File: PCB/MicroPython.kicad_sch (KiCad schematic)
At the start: 70 parts, among them J1 Conn_01x08, J10 USB4105-GF-A, J11 Micro_SD_Card, J2 Conn_01x08, J3 Conn_01x08, J4 Conn_01x08, J5 Conn_02x04_Odd_Even, J6 Conn_01x08, J7 Conn_01x08, J8 Conn_02x03_Odd_Even, J9 Conn_01x02, Q1 DMP2160UW, SW1 SW_MEC_5E, SW2 SW_MEC_5E, U1 STM32F405RGT6, U2 MCP1700T, U3 MIC2005A-1YM5, U4 FXLS8971CFR1, Y1 12 MHz, Y2 32.768 kHz

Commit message: actualizado/modificado nome de projecto - MicroPython
- nome alterado para estar de acordo com folder de Projecto & Repositório no GitHub
- desenho ainda em desenvolvimento
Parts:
- removed C3: 2u2, Capacitor_SMD:C_0603_1608Metric, symbol Device:C_Small
- C9: now not fitted; now left out of the parts list
- J11: footprint PyBoard FootprintLib:47571-0001_MOL -> MicroPython FootprintLib:47571-0001_MOL
- U1: symbol PyBoard SymbLib:STM32F405RGT6 -> MicroPython SymbLib:STM32F405RGT6
- U4: footprint PyBoard FootprintLib:LQFN-12-3x3mm_P0.65mm -> MicroPython FootprintLib:LQFN-12-3x3mm_P0.65mm; symbol PyBoard SymbLib:FXLS8971CFR1 -> MicroPython SymbLib:FXLS8971CFR1; now not fitted; now left out of the parts list
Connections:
- net PA11-DM renamed USB_N
- net PA12-DP renamed USB_P
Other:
- note added: ". 32kHz crystal used 'only' to SD-Card . since SD-card won't be used, does Crystal needs to be assmbled? . isn't OSC-pins needed to outher micro functionalities?"
- note added: "PA10-ID: USB 2.0 ID with no pin conn on USB-C will create USB fw-trouble?"
- note added: "rest of JTAG & SW debug available on bottom connector Note: LED resistors may need to be removed for debug (tbd) (note from v.1.1) programming pins PA13 PA14 PA15 PB4 connected to LEDs trouble??"
- note removed: "PA10-ID: USB ID sem conn nesta ficha afecta algo com o fw?"
- note removed: "programming pins PA13 PA14 PA15 PB4 connected to LEDs trouble??"
- note removed: "rest of JTAG & SW debug available on bottom connector Note: LED resistors may need to be removed for debug (tbd) (note from v.1.1)"

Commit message: MicroPython v.1.0
MicroPython v.1.0
- DRC=0
- em falta alguns novos OEPSPN
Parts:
- C1, C4, C5: MPN (none) -> GRM188R61E225KA12D; OEPSPN (none) -> OEPS010075
- C11, C12, C13, C14, C15, C18, C20, C6, C9: MPN (none) -> CGA2B3X7R1H104K050BB; OEPSPN (none) -> OEPS010016
- C16, C17, C2: MPN (none) -> C1608X6S1C475K080AC; OEPSPN (none) -> OEPS010018
- C21, C22, C7, C8: value 12p -> 12pF; MPN (none) -> GRM1555C1H120JA01D; OEPSPN (none) -> OEPS01????
- D1: value MSE1PB-M3/89A -> BAS316-TP; footprint Diode_SMD:D_SOD-123 -> Diode_SMD:D_SOD-323; MPN (none) -> BAS316-TP; OEPSPN (none) -> OEPS030001; notes (none) -> original part MSE1PB-M3/89A
- D2: MPN (none) -> 5975004407F; OEPSPN (none) -> OEPS030006
- D3: MPN (none) -> LSM0603453V; OEPSPN (none) -> OEPS030032
- D4: MPN (none) -> 5990040007F; OEPSPN (none) -> OEPS03????
- D5: MPN (none) -> 5988D90107F; OEPSPN (none) -> OEPS03????
- FB1: value 1k -> 1k@100MHz; footprint Inductor_SMD:L_0603_1608Metric -> Inductor_SMD:L_0402_1005Metric; MPN (none) -> BLM15HD102SN1D; OEPSPN (none) -> OEPS040013
- J1, J2, J6, J7, J8: MPN (none) -> -; OEPSPN (none) -> n.a.
- J3, J4, J5: MPN (none) -> -; OEPSPN (none) -> n.a.; now left out of the parts list
- J9: footprint Connector_PinHeader_1.00mm:PinHeader_1x02_P1.00mm_Vertical -> Connector_PinHeader_2.54mm:PinHeader_1x02_P2.54mm_Vertical; MPN (none) -> -; OEPSPN (none) -> n.a.; now left out of the parts list
- Q1: value DMP2160UW -> PMF170XP; MPN (none) -> PMF170XP,115; OEPSPN (none) -> OEPS060012; notes (none) -> original part: DMP2160UW
- R1, R10, R11, R19: MPN (none) -> AC0402FR-07100KL; OEPSPN (none) -> OEPS020051
- R12, R13, R14, R15, R16, R21: MPN (none) -> CRCW04021M00FKED; OEPSPN (none) -> OEPS020026
- R2, R6, R7, R8: MPN (none) -> CRCW0402560RFKED; OEPSPN (none) -> OEPS02????
- R20, R9: value 220R -> 270R; MPN (none) -> CRCW0402270RFKEDC; OEPSPN (none) -> OEPS020060
- R22: MPN (none) -> ERJ-2RKF1002X; OEPSPN (none) -> OEPS020013
- R3, R4: MPN (none) -> RMCF0402FT27R0; OEPSPN (none) -> OEPS020170
- SW1, SW2: value SW_MEC_5E -> SW_SPST; footprint Button_Switch_SMD:SW_Push_1P1T_NO_CK_KMR2 -> Button_Switch_SMD:SW_SPST_TL3305B; MPN (none) -> TL3305BF260QG; OEPSPN (none) -> OEPS100061
- U1: MPN (none) -> STM32F405RGT6; OEPSPN (none) -> OEPS08????
- U3: MPN (none) -> MIC2005A-1YM5-TR; OEPSPN (none) -> OEPS08????
- U4: OEPSPN TBD -> n.a.
- renumbered Y1 to X1, Y2 to X2
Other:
- moved on the sheet: J1, J2, J3, J4, J5, J6, J7, J8, R20

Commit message: Update MicroPython.kicad_sch
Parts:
- J8: now left out of the parts list
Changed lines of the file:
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@@
 		(unit 1)
 		(exclude_from_sim no)
-		(in_bom yes)
+		(in_bom no)
 		(on_board yes)
 		(dnp no)

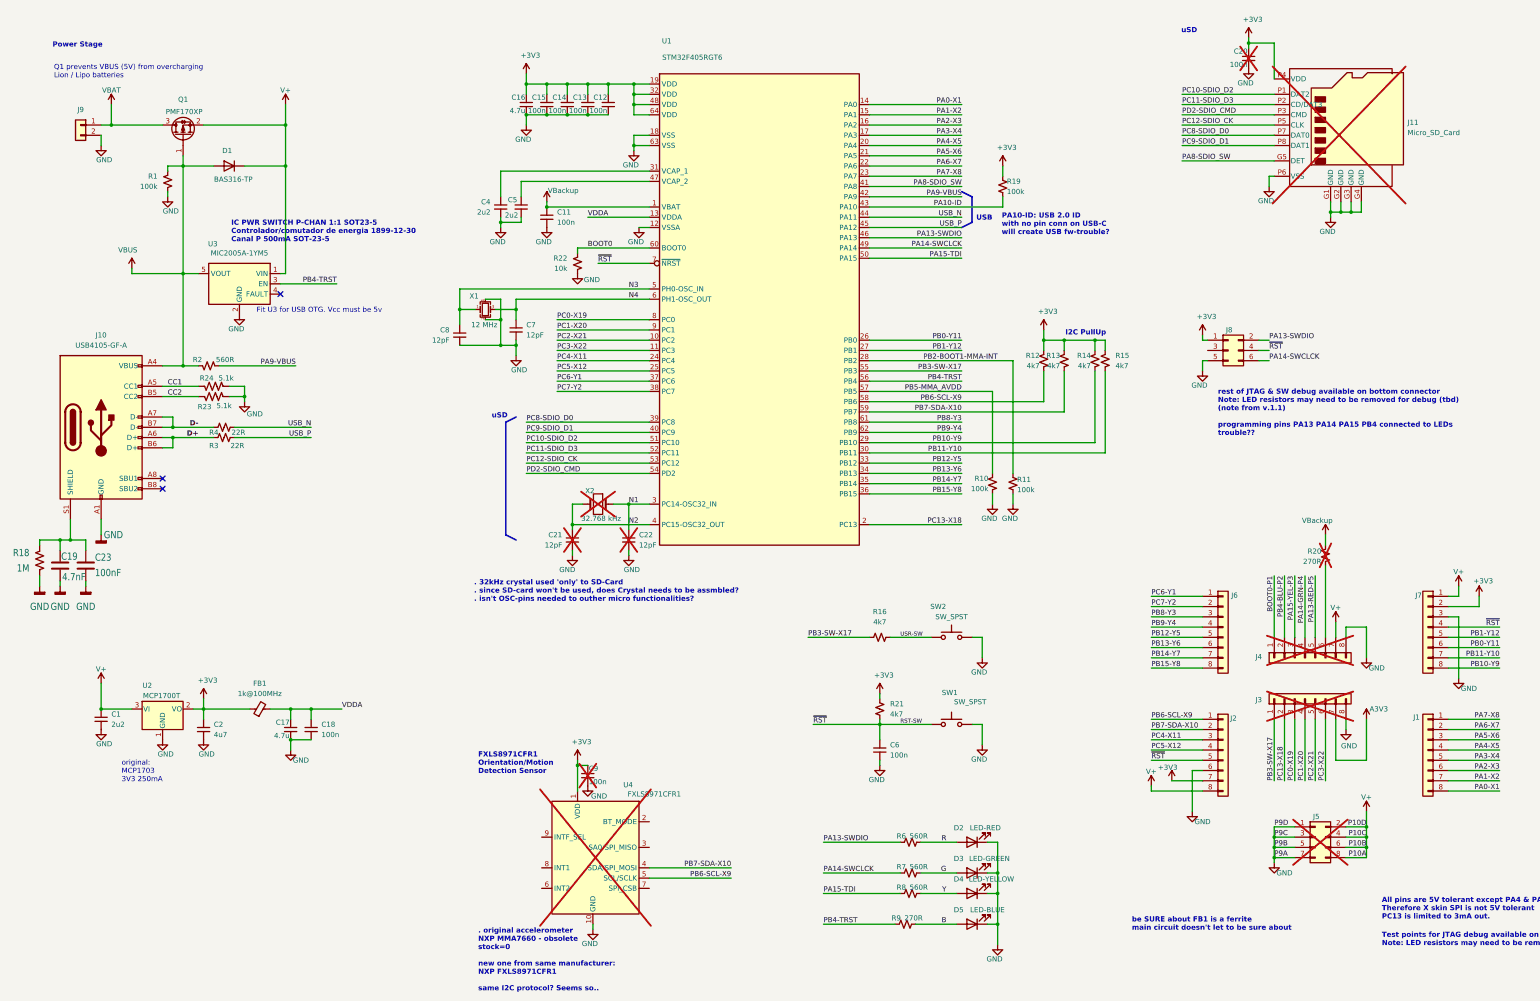
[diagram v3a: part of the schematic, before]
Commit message: MicroPhython v.1.0
- maior alterações a nivel do rail de PowerIn
- retirado a andar de PFET - em versões anteriores e posteriores à PCB v.1.1 estes andares não exixtiam
- realocação & re-routing na PCB do andar de PowerIn
- DRC=0
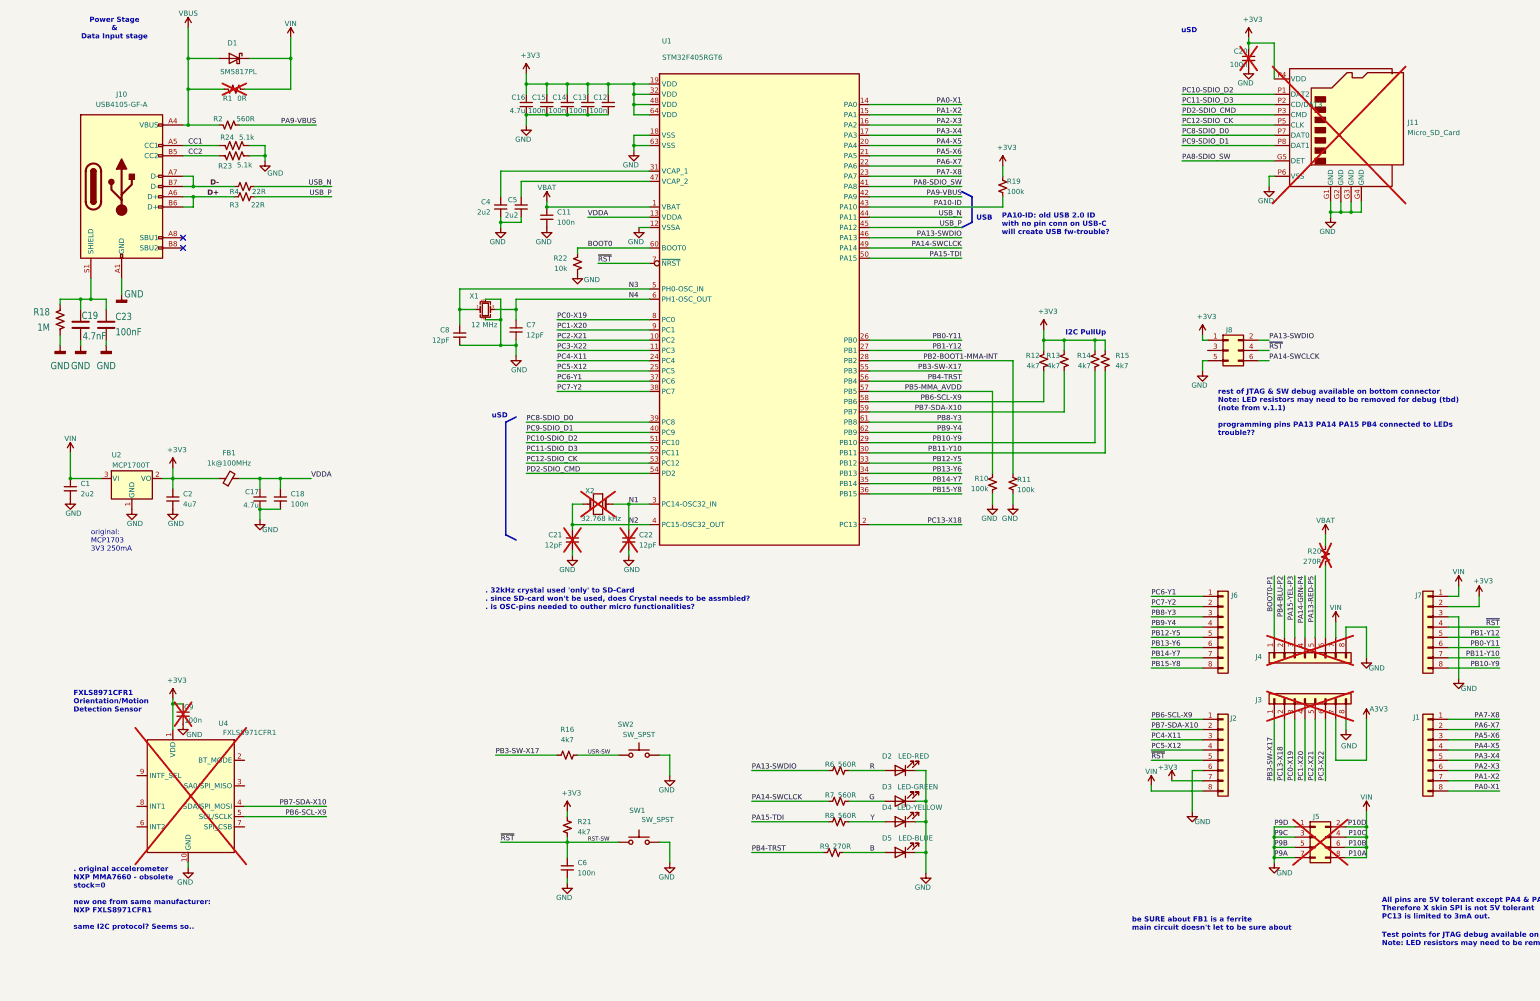
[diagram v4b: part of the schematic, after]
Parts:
- removed J9: Conn_01x02, Connector_PinHeader_2.54mm:PinHeader_1x02_P2.54mm_Vertical, symbol Connector_Generic:Conn_01x02
- removed Q1: PMF170XP, Package_TO_SOT_SMD:SOT-23, symbol Transistor_FET:DMP3099L
- removed U3: MIC2005A-1YM5, Package_TO_SOT_SMD:SOT-23-5, symbol Power_Management:MIC2090-2YM5
- D1: value BAS316-TP -> SM5817PL; footprint Diode_SMD:D_SOD-323 -> Diode_SMD:D_SOD-123F; symbol Diode:1N4148W -> Device:D_Schottky; MPN BAS316-TP -> SM5817PL-TP; OEPSPN OEPS030001 -> OEPS030030; notes original part MSE1PB-M3/89A -> original part: 1N5819
- R1: value 100k -> 0R; MPN AC0402FR-07100KL -> RC0402JR-070RL; OEPSPN OEPS020051 -> OEPS020001; now not fitted; now left out of the parts list
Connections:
- net VBackup is gone; now on net VBAT: C11.1, R20.1, U1.1 (VBAT)
- net GND: no longer R1.2
- net V+ renamed VIN
- net VIN: now also R1.2
- no-connect marks 3 -> 2
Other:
- note added: ". 32kHz crystal used 'only' to SD-Card . since SD-card won't be used, does Crystal needs to be assmbled? . is OSC-pins needed to outher micro functionalities?"
- note added: "PA10-ID: old USB 2.0 ID with no pin conn on USB-C will create USB fw-trouble?"
- note added: "Power Stage & Data Input stage"
- note removed: ". 32kHz crystal used 'only' to SD-Card . since SD-card won't be used, does Crystal needs to be assmbled? . isn't OSC-pins needed to outher micro functionalities?"
- note removed: "Fit U3 for USB OTG. Vcc must be 5v"
- note removed: "IC PWR SWITCH P-CHAN 1:1 SOT23-5 Controlador/comutador de energia 1899-12-30 Canal P 500mA SOT-23-5"
- note removed: "PA10-ID: USB 2.0 ID with no pin conn on USB-C will create USB fw-trouble?"
- note removed: "Power Stage"
- note removed: "Q1 prevents VBUS (5V) from overcharging Lion / Lipo batteries"
- moved on the sheet: C1, C17, C18, C19, C2, C23, C6, C9, D1, D2, D3, D4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

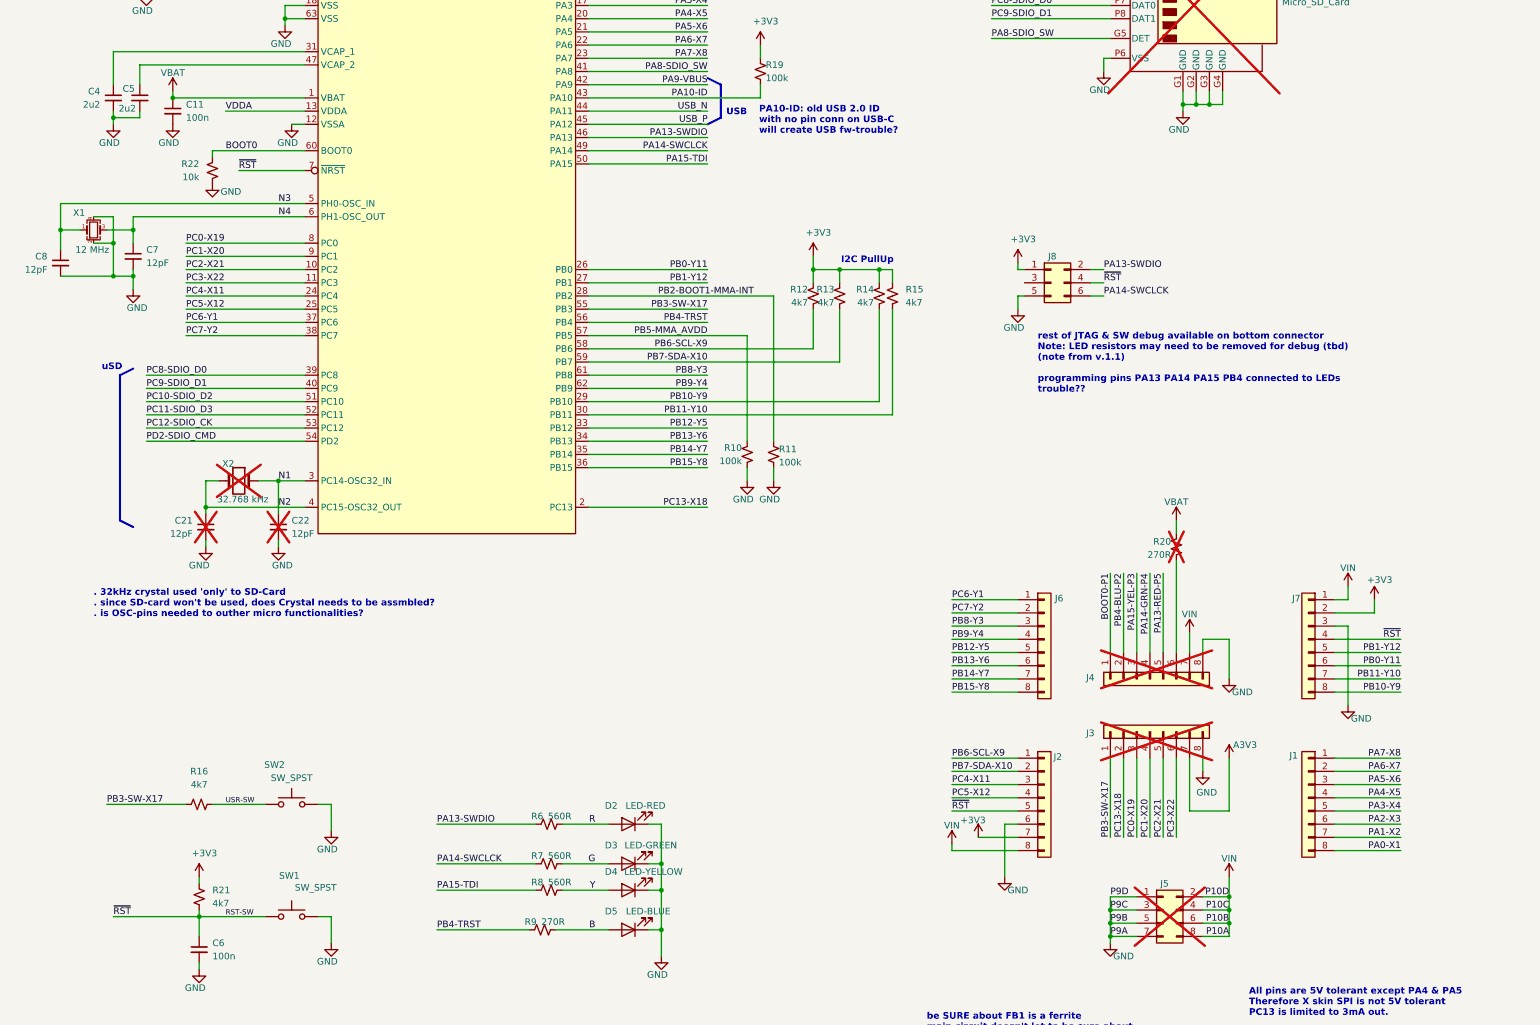
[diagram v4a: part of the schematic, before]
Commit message: ficheiros de produção gerados
- todos os componentes com OEPS & MPN
- gerados ficheiros de produção \production
- gerada BOM
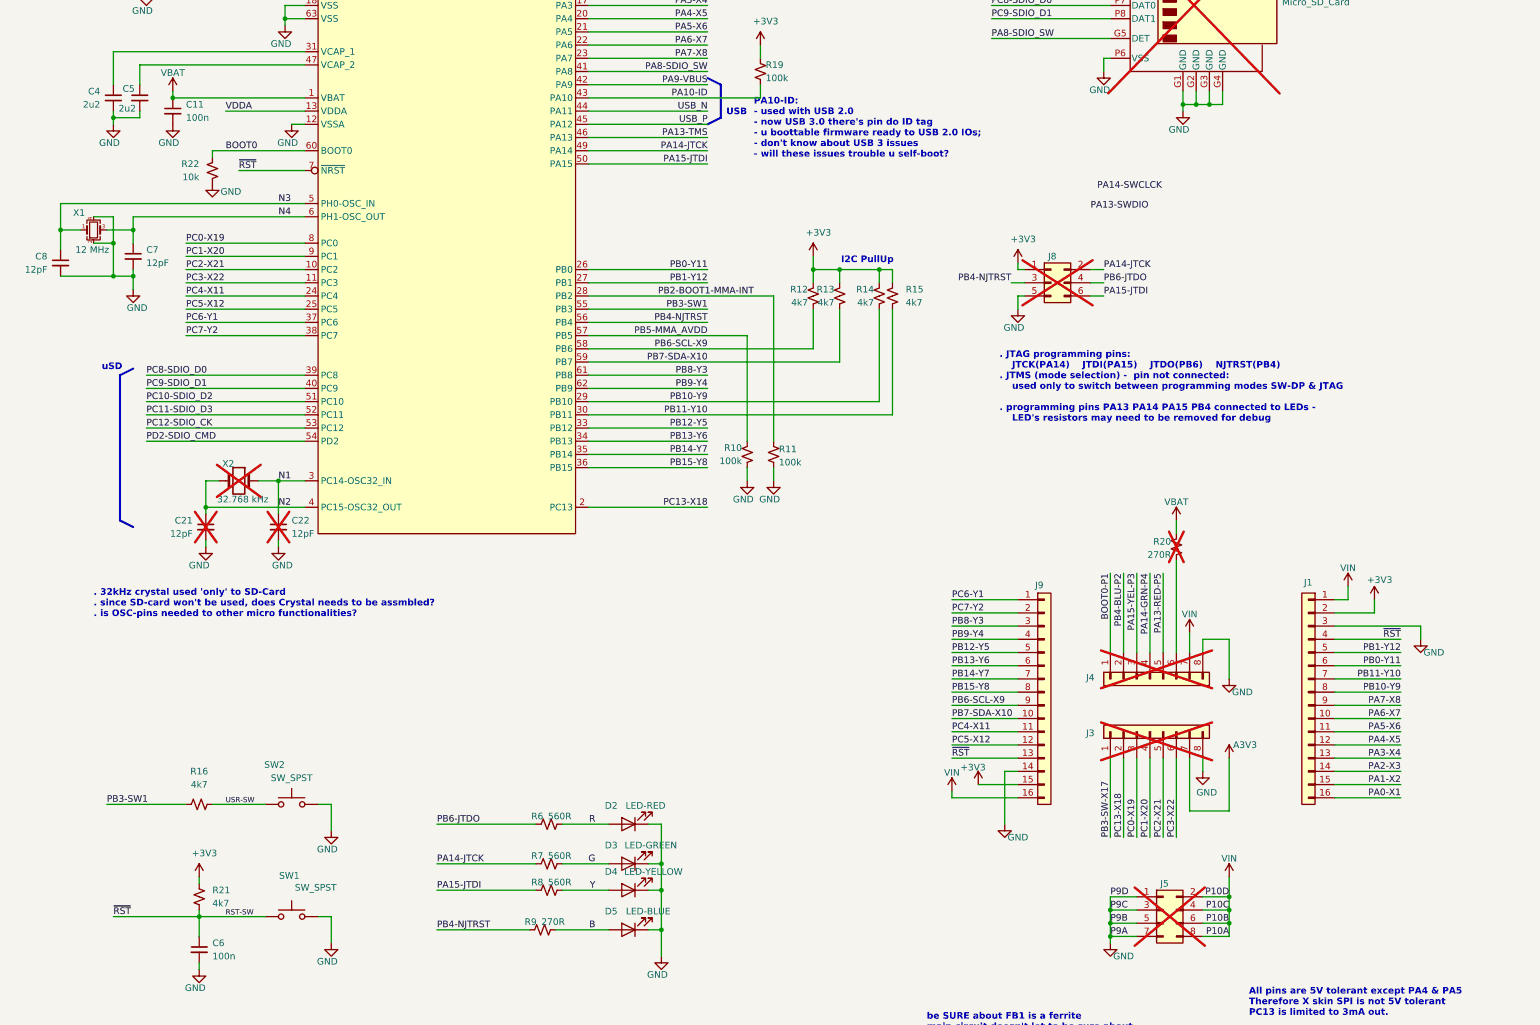
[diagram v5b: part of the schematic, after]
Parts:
- removed J1, J2, J6, J7: Conn_01x08, Connector_PinHeader_2.54mm:PinHeader_1x08_P2.54mm_Vertical, symbol Connector_Generic:Conn_01x08
- added J1, J9: Conn_01x08, Connector_PinHeader_2.54mm:PinHeader_1x16_P2.54mm_Vertical, symbol Connector_Generic:Conn_01x16
- C20, J11, R20: now left out of the parts list
- C21, C22, C7, C8: OEPSPN OEPS01???? -> OEPS010086
- D4: OEPSPN OEPS03???? -> OEPS030043
- D5: OEPSPN OEPS03???? -> OEPS030042
- J3, J4: MPN - -> CES-116-01-T-S; OEPSPN n.a. -> OEPS070110
- J8: now not fitted
- R2, R6, R7, R8: OEPSPN OEPS02???? -> OEPS020193
- U1: OEPSPN OEPS08???? -> OEPS080178
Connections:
- net PB4-TRST is gone; now on net PB4-NJTRST: R9.1, U1.56 (PB4)
- net +3V3: now also J1.2 (Pin_2), J9.15 (Pin_15)
- net GND: now also J1.3 (Pin_3), J9.14 (Pin_14)
- net PA0-X1: now also J1.16 (Pin_16)
- net PA1-X2: now also J1.15 (Pin_15)
- net PA13-SWDIO: no longer J8.2 (Pin_2), R6.1, U1.46 (PA13)
- net PA14-SWCLCK: no longer J8.6 (Pin_6), R7.1, U1.49 (PA14)
- net PA2-X3: now also J1.14 (Pin_14)
- net PA3-X4: now also J1.13 (Pin_13)
- net PA4-X5: now also J1.12 (Pin_12)
- net PA5-X6: now also J1.11 (Pin_11)
- net PA6-X7: now also J1.10 (Pin_10)
- net PA7-X8: now also J1.9 (Pin_9)
- net PB0-Y11: now also J1.6 (Pin_6)
- net PB1-Y12: now also J1.5 (Pin_5)
- net PB10-Y9: now also J1.8 (Pin_8)
- net PB11-Y10: now also J1.7 (Pin_7)
- net PB12-Y5: now also J9.5 (Pin_5)
- net PB13-Y6: now also J9.6 (Pin_6)
- net PB14-Y7: now also J9.7 (Pin_7)
- net PB15-Y8: now also J9.8 (Pin_8)
- net PB3-SW-X17: no longer R16.1, U1.55 (PB3)
- net PB6-SCL-X9: now also J9.9 (Pin_9)
- net PB7-SDA-X10: now also J9.10 (Pin_10)
- net PB8-Y3: now also J9.3 (Pin_3)
- net PB9-Y4: now also J9.4 (Pin_4)
- net PC4-X11: now also J9.11 (Pin_11)
- net PC5-X12: now also J9.12 (Pin_12)
- net PC6-Y1: now also J9.1 (Pin_1)
- net PC7-Y2: now also J9.2 (Pin_2)
- net RST-SW: now also J1.4 (Pin_4), J9.13 (Pin_13); no longer J8.4 (Pin_4)
- net VIN: now also J1.1 (Pin_1), J9.16 (Pin_16)
- net PB4-NJTRST: now reaches J8.3 (Pin_3)
- net PA15-TDI renamed PA15-JTDI
- net PA15-JTDI: now also J8.6 (Pin_6)
- new net PA13-TMS: U1.46 (PA13)
- new net PA14-JTCK: J8.2 (Pin_2), R7.1, U1.49 (PA14)
- new net PB3-SW1: R16.1, U1.55 (PB3)
- new net PB6-JTDO: J8.4 (Pin_4), R6.1
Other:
- note added: ". 32kHz crystal used 'only' to SD-Card . since SD-card won't be used, does Crystal needs to be assmbled? . is OSC-pins needed to other micro functionalities?"
- note added: ". JTAG programming pins: JTCK(PA14) JTDI(PA15) JTDO(PB6) NJTRST(PB4) . JTMS (mode selection) - pin not connected: used only to switch between programming modes SW-DP & JTAG . programming pins PA13 PA14 PA15 PB4 connected to LEDs - LED's resistors may need to be removed for debug"
- note added: "PA10-ID: - used with USB 2.0 - now USB 3.0 there's pin do ID tag - u boottable firmware ready to USB 2.0 IOs; - don't know about USB 3 issues - will these issues trouble u self-boot?"
- note removed: ". 32kHz crystal used 'only' to SD-Card . since SD-card won't be used, does Crystal needs to be assmbled? . is OSC-pins needed to outher micro functionalities?"
- note removed: "PA10-ID: old USB 2.0 ID with no pin conn on USB-C will create USB fw-trouble?"
- note removed: "rest of JTAG & SW debug available on bottom connector Note: LED resistors may need to be removed for debug (tbd) (note from v.1.1) programming pins PA13 PA14 PA15 PB4 connected to LEDs trouble??"
